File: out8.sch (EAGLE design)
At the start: 38 parts, among them IC1 74HC595N, K301 S202S02, K302 S202S02, K303 S202S02, K304 S202S02, K305 S202S02, K306 S202S02, K307 S202S02, K308 S202S02

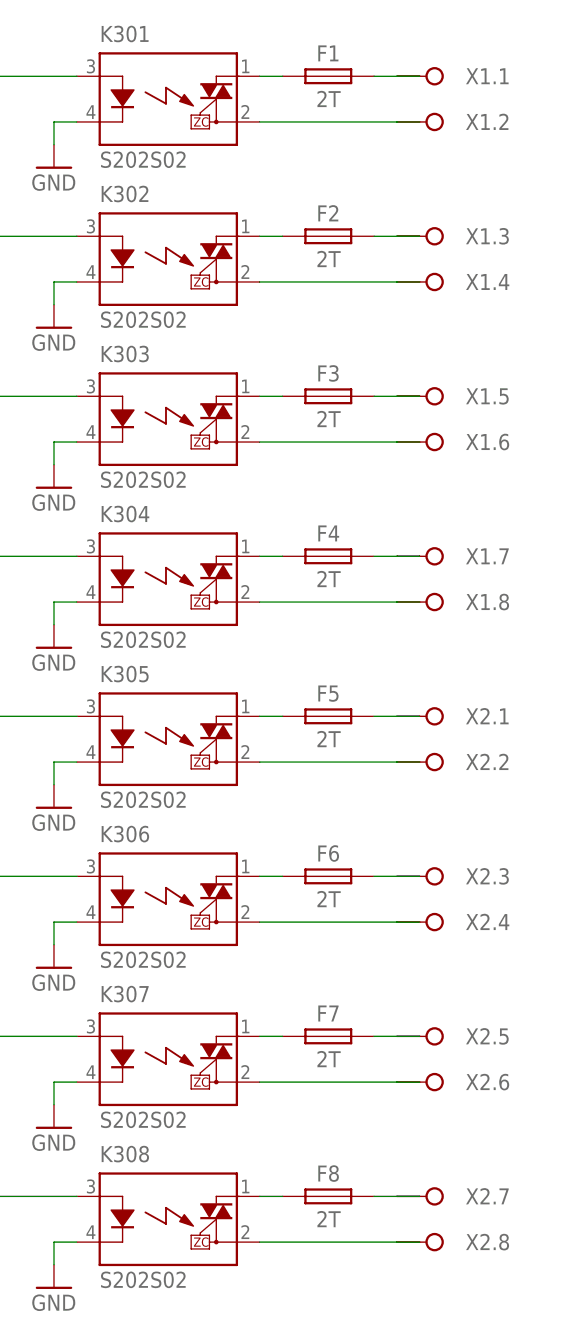
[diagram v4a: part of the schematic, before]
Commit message: Anschlussklemmen ausgetauscht
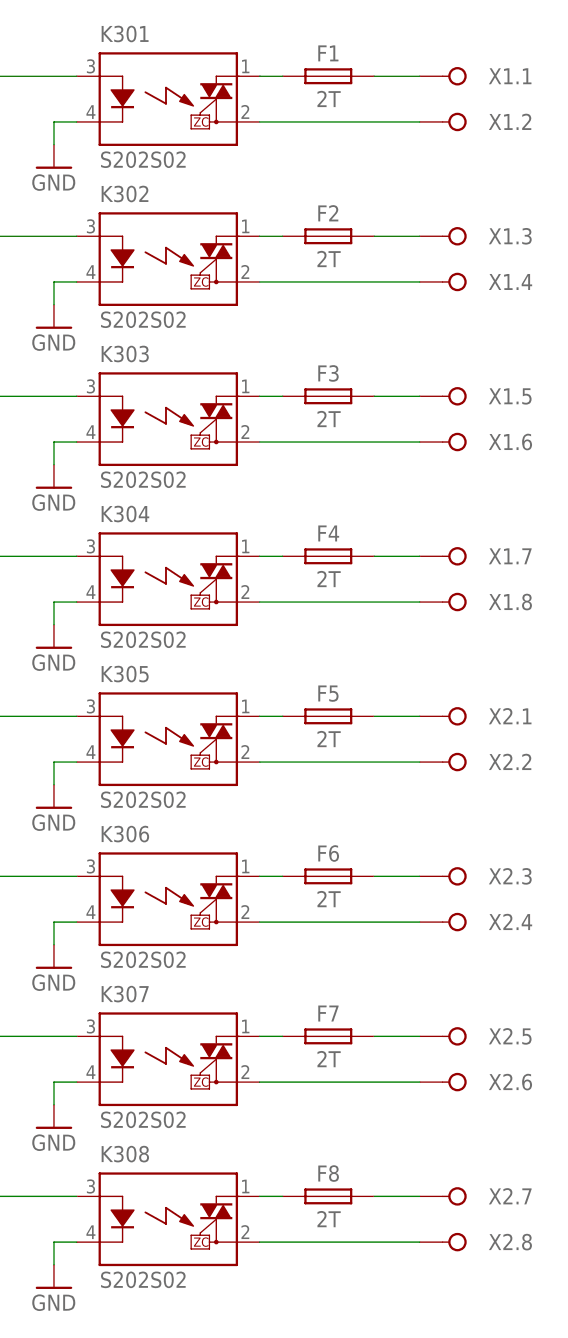
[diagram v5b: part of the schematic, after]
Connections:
- net N$10: no longer X1.1.B
- net N$11: no longer X1.2.B
- net N$13: no longer X1.3.B
- net N$14: no longer X1.4.B
- net N$16: no longer X1.5.B
- net N$25: no longer X1.6.B
- net N$27: no longer X1.7.B
- net N$28: no longer X1.8.B
- net N$30: no longer X2.1.B
- net N$31: no longer X2.2.B
- net N$33: no longer X2.3.B
- net N$34: no longer X2.4.B
- net N$36: no longer X2.5.B
- net N$37: no longer X2.6.B
- net N$39: no longer X2.7.B
- net N$40: no longer X2.8.B
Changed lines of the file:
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@@
 <part name="F7" library="sicherung" deviceset="TR5" device="" value="2T"/>
 <part name="F8" library="sicherung" deviceset="TR5" device="" value="2T"/>
-<part name="X1" library="anschluss" deviceset="WAGO_236-408" device=""/>
-<part name="X2" library="anschluss" deviceset="WAGO_236-408" device=""/>
 <part name="GND1" library="versorgung" deviceset="GND" device=""/>
 <part name="P+1" library="versorgung" deviceset="+5V" device=""/>
@@
 <part name="IC1" library="74xx-eu" deviceset="74*595" device="N" technology="HC"/>
 <part name="GND2" library="versorgung" deviceset="GND" device=""/>
+<part name="X1" library="anschluss" deviceset="WAGO_236-408" device=""/>
+<part name="X2" library="anschluss" deviceset="WAGO_236-408" device=""/>
 </parts>
 <sheets>
@@
 <instance part="F7" gate="1" x="147.32" y="38.1"/>
 <instance part="F8" gate="1" x="147.32" y="20.32"/>
-<instance part="X1" gate=".1" x="160.02" y="144.78" rot="R180"/>
-<instance part="X1" gate=".2" x="160.02" y="139.7" rot="R180"/>
-<instance part="X1" gate=".3" x="160.02" y="127" rot="R180"/>
-<instance part="X1" gate=".4" x="160.02" y="121.92" rot="R180"/>
-<instance part="X1" gate=".5" x="160.02" y="109.22" rot="R180"/>
-<instance part="X1" gate=".6" x="160.02" y="104.14" rot="R180"/>
-<instance part="X1" gate=".7" x="160.02" y="91.44" rot="R180"/>
-<instance part="X1" gate=".8" x="160.02" y="86.36" rot="R180"/>
-<instance part="X2" gate=".1" x="160.02" y="73.66" rot="R180"/>
-<instance part="X2" gate=".2" x="160.02" y="68.58" rot="R180"/>
-<instance part="X2" gate=".3" x="160.02" y="55.88" rot="R180"/>
-<instance part="X2" gate=".4" x="160.02" y="50.8" rot="R180"/>
-<instance part="X2" gate=".5" x="160.02" y="38.1" rot="R180"/>
-<instance part="X2" gate=".6" x="160.02" y="33.02" rot="R180"/>
-<instance part="X2" gate=".7" x="160.02" y="20.32" rot="R180"/>
-<instance part="X2" gate=".8" x="160.02" y="15.24" rot="R180"/>
 <instance part="GND1" gate="1" x="25.4" y="30.48"/>
 <instance part="P+1" gate="1" x="25.4" y="119.38"/>
@@
 <instance part="GND2" gate="1" x="33.02" y="63.5"/>
 <instance part="IC1" gate="P" x="53.34" y="116.84"/>
+<instance part="X1" gate=".1" x="162.56" y="144.78" rot="R180"/>
+<instance part="X1" gate=".2" x="162.56" y="139.7" rot="R180"/>
+<instance part="X1" gate=".3" x="162.56" y="127" rot="R180"/>
+<instance part="X1" gate=".4" x="162.56" y="121.92" rot="R180"/>
+<instance part="X1" gate=".5" x="162.56" y="109.22" rot="R180"/>
+<instance part="X1" gate=".6" x="162.56" y="104.14" rot="R180"/>
+<instance part="X1" gate=".7" x="162.56" y="91.44" rot="R180"/>
+<instance part="X1" gate=".8" x="162.56" y="86.36" rot="R180"/>
+<instance part="X2" gate=".1" x="162.56" y="73.66" rot="R180"/>
+<instance part="X2" gate=".2" x="162.56" y="68.58" rot="R180"/>
+<instance part="X2" gate=".3" x="162.56" y="55.88" rot="R180"/>
+<instance part="X2" gate=".4" x="162.56" y="50.8" rot="R180"/>
+<instance part="X2" gate=".5" x="162.56" y="38.1" rot="R180"/>
+<instance part="X2" gate=".6" x="162.56" y="33.02" rot="R180"/>
+<instance part="X2" gate=".7" x="162.56" y="20.32" rot="R180"/>
+<instance part="X2" gate=".8" x="162.56" y="15.24" rot="R180"/>
 </instances>
 <busses>
@@
 <segment>
 <pinref part="F1" gate="1" pin="2"/>
+<wire x1="152.4" y1="144.78" x2="157.48" y2="144.78" width="0.1524" layer="91"/>
 <pinref part="X1" gate=".1" pin="A"/>
-<wire x1="152.4" y1="144.78" x2="154.94" y2="144.78" width="0.1524" layer="91"/>
-<pinref part="X1" gate=".1" pin="B"/>
-<wire x1="154.94" y1="144.78" x2="157.48" y2="144.78" width="0.1524" layer="91"/>
 </segment>
 </net>
@@
 <segment>
 <pinref part="K301" gate="G$1" pin="DS2"/>
+<wire x1="139.7" y1="139.7" x2="157.48" y2="139.7" width="0.1524" layer="91"/>
 <pinref part="X1" gate=".2" pin="A"/>
-<wire x1="139.7" y1="139.7" x2="154.94" y2="139.7" width="0.1524" layer="91"/>
-<pinref part="X1" gate=".2" pin="B"/>
-<wire x1="154.94" y1="139.7" x2="157.48" y2="139.7" width="0.1524" layer="91"/>
 </segment>
 </net>
@@
 <segment>
 <pinref part="F2" gate="1" pin="2"/>
+<wire x1="152.4" y1="127" x2="157.48" y2="127" width="0.1524" layer="91"/>
 <pinref part="X1" gate=".3" pin="A"/>
-<wire x1="152.4" y1="127" x2="154.94" y2="127" width="0.1524" layer="91"/>
-<pinref part="X1" gate=".3" pin="B"/>
-<wire x1="154.94" y1="127" x2="157.48" y2="127" width="0.1524" layer="91"/>
 </segment>
 </net>
@@
 <segment>
 <pinref part="K302" gate="G$1" pin="DS2"/>
+<wire x1="139.7" y1="121.92" x2="157.48" y2="121.92" width="0.1524" layer="91"/>
 <pinref part="X1" gate=".4" pin="A"/>
-<wire x1="139.7" y1="121.92" x2="154.94" y2="121.92" width="0.1524" layer="91"/>
-<pinref part="X1" gate=".4" pin="B"/>
-<wire x1="154.94" y1="121.92" x2="157.48" y2="121.92" width="0.1524" layer="91"/>
 </segment>
 </net>
@@
 <segment>
 <pinref part="F3" gate="1" pin="2"/>
+<wire x1="152.4" y1="109.22" x2="157.48" y2="109.22" width="0.1524" layer="91"/>
 <pinref part="X1" gate=".5" pin="A"/>
-<wire x1="152.4" y1="109.22" x2="154.94" y2="109.22" width="0.1524" layer="91"/>
-<pinref part="X1" gate=".5" pin="B"/>
-<wire x1="154.94" y1="109.22" x2="157.48" y2="109.22" width="0.1524" layer="91"/>
 </segment>
 </net>
@@
 <segment>
 <pinref part="K303" gate="G$1" pin="DS2"/>
+<wire x1="139.7" y1="104.14" x2="157.48" y2="104.14" width="0.1524" layer="91"/>
 <pinref part="X1" gate=".6" pin="A"/>
-<wire x1="139.7" y1="104.14" x2="154.94" y2="104.14" width="0.1524" layer="91"/>
-<pinref part="X1" gate=".6" pin="B"/>
-<wire x1="154.94" y1="104.14" x2="157.48" y2="104.14" width="0.1524" layer="91"/>
 </segment>
 </net>
@@
 <segment>
 <pinref part="F4" gate="1" pin="2"/>
+<wire x1="152.4" y1="91.44" x2="157.48" y2="91.44" width="0.1524" layer="91"/>
 <pinref part="X1" gate=".7" pin="A"/>
-<wire x1="152.4" y1="91.44" x2="154.94" y2="91.44" width="0.1524" layer="91"/>
-<pinref part="X1" gate=".7" pin="B"/>
-<wire x1="154.94" y1="91.44" x2="157.48" y2="91.44" width="0.1524" layer="91"/>
 </segment>
 </net>
@@
 <segment>
 <pinref part="K304" gate="G$1" pin="DS2"/>
+<wire x1="139.7" y1="86.36" x2="157.48" y2="86.36" width="0.1524" layer="91"/>
 <pinref part="X1" gate=".8" pin="A"/>
-<wire x1="139.7" y1="86.36" x2="154.94" y2="86.36" width="0.1524" layer="91"/>
-<pinref part="X1" gate=".8" pin="B"/>
-<wire x1="154.94" y1="86.36" x2="157.48" y2="86.36" width="0.1524" layer="91"/>
 </segment>
 </net>
@@
 <segment>
 <pinref part="F5" gate="1" pin="2"/>
+<wire x1="152.4" y1="73.66" x2="157.48" y2="73.66" width="0.1524" layer="91"/>
 <pinref part="X2" gate=".1" pin="A"/>
-<wire x1="152.4" y1="73.66" x2="154.94" y2="73.66" width="0.1524" layer="91"/>
-<pinref part="X2" gate=".1" pin="B"/>
-<wire x1="154.94" y1="73.66" x2="157.48" y2="73.66" width="0.1524" layer="91"/>
 </segment>
 </net>
@@
 <segment>
 <pinref part="K305" gate="G$1" pin="DS2"/>
+<wire x1="139.7" y1="68.58" x2="157.48" y2="68.58" width="0.1524" layer="91"/>
 <pinref part="X2" gate=".2" pin="A"/>
-<wire x1="139.7" y1="68.58" x2="154.94" y2="68.58" width="0.1524" layer="91"/>
-<pinref part="X2" gate=".2" pin="B"/>
-<wire x1="154.94" y1="68.58" x2="157.48" y2="68.58" width="0.1524" layer="91"/>
 </segment>
 </net>
@@
 <segment>
 <pinref part="F6" gate="1" pin="2"/>
+<wire x1="152.4" y1="55.88" x2="157.48" y2="55.88" width="0.1524" layer="91"/>
 <pinref part="X2" gate=".3" pin="A"/>
-<wire x1="152.4" y1="55.88" x2="154.94" y2="55.88" width="0.1524" layer="91"/>
-<pinref part="X2" gate=".3" pin="B"/>
-<wire x1="154.94" y1="55.88" x2="157.48" y2="55.88" width="0.1524" layer="91"/>
 </segment>
 </net>
@@
 <segment>
 <pinref part="K306" gate="G$1" pin="DS2"/>
+<wire x1="139.7" y1="50.8" x2="157.48" y2="50.8" width="0.1524" layer="91"/>
 <pinref part="X2" gate=".4" pin="A"/>
-<wire x1="139.7" y1="50.8" x2="154.94" y2="50.8" width="0.1524" layer="91"/>
-<pinref part="X2" gate=".4" pin="B"/>
-<wire x1="154.94" y1="50.8" x2="157.48" y2="50.8" width="0.1524" layer="91"/>
 </segment>
 </net>
@@
 <segment>
 <pinref part="F7" gate="1" pin="2"/>
+<wire x1="152.4" y1="38.1" x2="157.48" y2="38.1" width="0.1524" layer="91"/>
 <pinref part="X2" gate=".5" pin="A"/>
-<wire x1="152.4" y1="38.1" x2="154.94" y2="38.1" width="0.1524" layer="91"/>
-<pinref part="X2" gate=".5" pin="B"/>
-<wire x1="154.94" y1="38.1" x2="157.48" y2="38.1" width="0.1524" layer="91"/>
 </segment>
 </net>
@@
 <segment>
 <pinref part="K307" gate="G$1" pin="DS2"/>
+<wire x1="139.7" y1="33.02" x2="157.48" y2="33.02" width="0.1524" layer="91"/>
 <pinref part="X2" gate=".6" pin="A"/>
-<wire x1="139.7" y1="33.02" x2="154.94" y2="33.02" width="0.1524" layer="91"/>
-<pinref part="X2" gate=".6" pin="B"/>
-<wire x1="154.94" y1="33.02" x2="157.48" y2="33.02" width="0.1524" layer="91"/>
 </segment>
 </net>
@@
 <segment>
 <pinref part="F8" gate="1" pin="2"/>
+<wire x1="152.4" y1="20.32" x2="157.48" y2="20.32" width="0.1524" layer="91"/>
 <pinref part="X2" gate=".7" pin="A"/>
-<wire x1="152.4" y1="20.32" x2="154.94" y2="20.32" width="0.1524" layer="91"/>
-<pinref part="X2" gate=".7" pin="B"/>
-<wire x1="154.94" y1="20.32" x2="157.48" y2="20.32" width="0.1524" layer="91"/>
 </segment>
 </net>
@@
 <segment>
 <pinref part="K308" gate="G$1" pin="DS2"/>
+<wire x1="139.7" y1="15.24" x2="157.48" y2="15.24" width="0.1524" layer="91"/>
 <pinref part="X2" gate=".8" pin="A"/>
-<wire x1="139.7" y1="15.24" x2="154.94" y2="15.24" width="0.1524" layer="91"/>
-<pinref part="X2" gate=".8" pin="B"/>
-<wire x1="154.94" y1="15.24" x2="157.48" y2="15.24" width="0.1524" layer="91"/>
-</segment>
-</net>
+</segment>
+</net>
